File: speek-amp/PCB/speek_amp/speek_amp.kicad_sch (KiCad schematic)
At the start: 5 parts

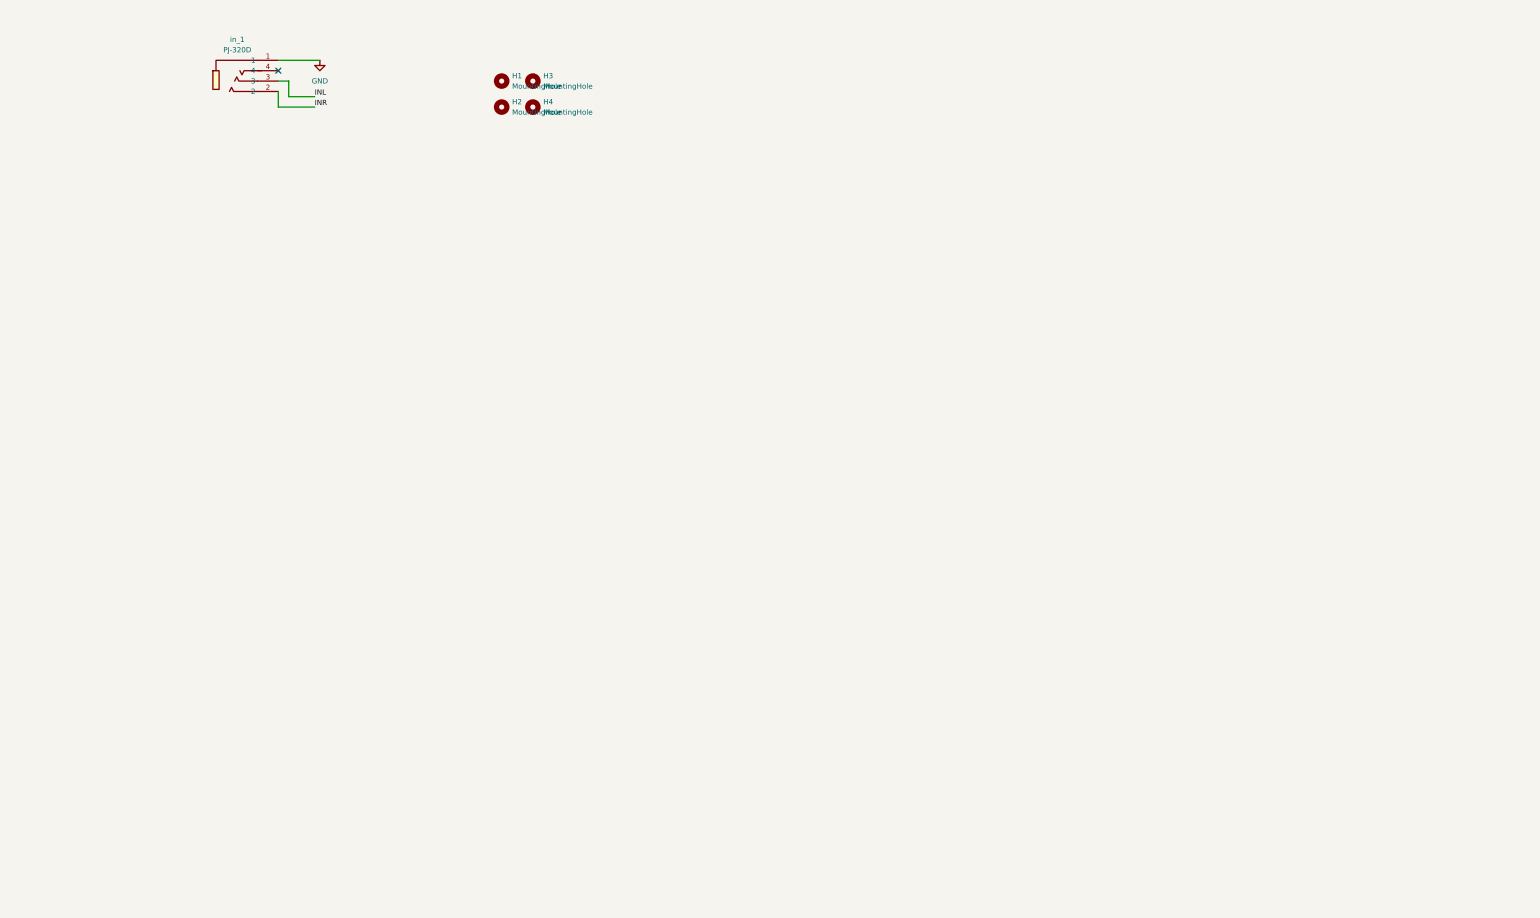
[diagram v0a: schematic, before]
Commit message: the speek amp schematic
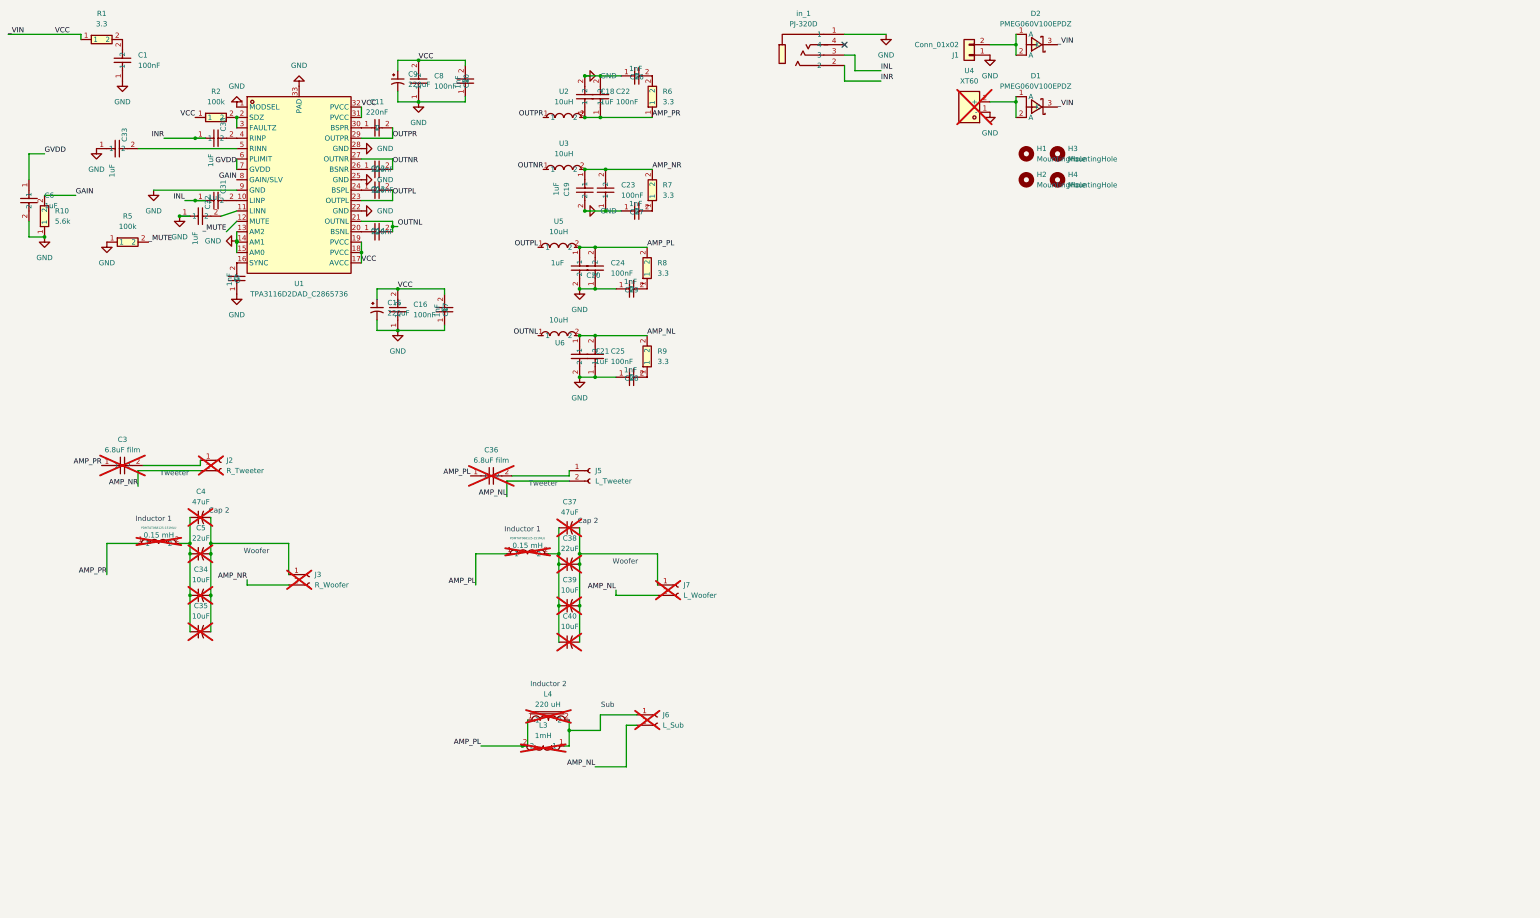
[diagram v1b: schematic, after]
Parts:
- added C1, C16, C22, C23, C24, C25, C8: 100nF, easyeda2kicad:C0402, symbol lcsc:CC0402KRX7R7BB104
- added C10, C17, C26, C27, C28, C29, C7: 1nF, easyeda2kicad:C0402, symbol lcsc:CL05B102KB5NNNC
- added C11, C12, C13, C14: 220nF, easyeda2kicad:C0402, symbol lcsc:CL05B224KO5NNNC
- added C15, C9: 220uF, easyeda2kicad:CAP-SMD_BD8.0-L8.3-W8.3-FD, symbol Device:C_Polarized_Small_US
- added C18, C19, C20, C21, C30, C31, C32, C33, C6: 1uF, easyeda2kicad:C0402, symbol lcsc:CGA0402X5R105M100GT
- added C3, C36: 6.8uF film, easyeda2kicad:CAP-TH_L29.5-W12.7-P27.00-D0.8, symbol lcsc:W312G685JS8SA1C0EC
- added C34, C35, C39, C40: 10uF, Capacitor_THT:CP_Radial_D6.3mm_P2.50mm, symbol Device:C_Small_US
- added C37, C4: 47uF, Capacitor_THT:CP_Radial_D6.3mm_P2.50mm, symbol Device:C_Small_US
- added C38, C5: 22uF, Capacitor_THT:CP_Radial_D6.3mm_P2.50mm, symbol Device:C_Small_US
- added D1, D2: PMEG060V100EPDZ, easyeda2kicad:SOT1289_L5.8-W4.4-LS6.5-RD, symbol lcsc:PMEG060V100EPDZ
- added J1: Conn_01x02, Connector_JST:JST_VH_B2P-VH-B_1x02_P3.96mm_Vertical, symbol Connector_Generic:Conn_01x02
- added J2: R_Tweeter, Connector_PinHeader_2.54mm:PinHeader_1x02_P2.54mm_Vertical, symbol Connector:Conn_01x02_Socket
- added J3: R_Woofer, Connector_PinHeader_2.54mm:PinHeader_1x02_P2.54mm_Vertical, symbol Connector:Conn_01x02_Socket
- added J5: L_Tweeter, Connector_PinHeader_2.54mm:PinHeader_1x02_P2.54mm_Vertical, symbol Connector:Conn_01x02_Socket
- added J6: L_Sub, Connector_PinHeader_2.54mm:PinHeader_1x02_P2.54mm_Vertical, symbol Connector:Conn_01x02_Socket
- added J7: L_Woofer, Connector_PinHeader_2.54mm:PinHeader_1x02_P2.54mm_Vertical, symbol Connector:Conn_01x02_Socket
- added L3: 1mH, easyeda2kicad:IND-TH_L33.0-W21.0-P15.3-D1.0, symbol lcsc:PDMTAT3321-102MLG
- added L4: 220 uH, easyeda2kicad:IND-TH_BD22.3-P8.50-D1.2_XR068125TS221MHL8, symbol lcsc:XR068125TS221MHL8
- added R1, R6, R7, R8, R9: 3.3, easyeda2kicad:R0402, symbol lcsc:RC0402FR-073R3L
- added R10: 5.6k, easyeda2kicad:R0805, symbol lcsc:0805W8F5601T5E
- added R2, R5: 100k, easyeda2kicad:R0402, symbol lcsc:RC0402FR-07100KL
- added U1: TPA3116D2DAD_C2865736, easyeda2kicad:HTSSOP-32_L11.0-W6.1-P0.65-LS8.1-BL, symbol lcsc:TPA3116D2DAD_C2865736
- added U2, U3, U5, U6: 10uH, easyeda2kicad:IND-SMD_L7.2-W6.6_GPSR07X0, symbol lcsc:CYA0630-10UH
- added U4: XT60, easyeda2kicad:CONN-TH_XT60, symbol lcsc:XT60
- added U7, U8: PDMTAT068125-151MLU, easyeda2kicad:IND-TH_L23.0-W12.0-P8.00-D0.8, symbol lcsc:PDMTAT068125-151MLU
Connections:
- net GND: now also C1.1, C10.1, C15.2, C16.1, C17.1, C18.2, C19.2, C20.2, C21.2, C22.2, C23.1, C24.1, C25.1, C26.1, C27.1, C28.1, C29.1, C32.1, C33.1, C6.2, C7.1, C8.1, C9.2, J1.1 (Pin_1), R10.1, R5.1, U1.1 (MODSEL), U1.13 (AM2), U1.14 (AM1), U1.15 (AM0), U1.22 (GND), U1.25 (GND), U1.28 (GND), U1.33 (PAD), U1.9 (GND), U4.1 (-)
- net INL: now also C31.1
- net INR: now also C30.1
- new net: C13.1, U1.24 (BSPL)
- new net: C34.2, C35.2, C4.2, C5.2, J3.1 (Pin_1)
- new net: D1.1 (A), D1.2 (A), U4.2 (+)
- new net: C14.1, U1.20 (BSNL)
- new net: D2.1 (A), D2.2 (A), J1.2 (Pin_2)
- new net: C28.2, R9.1
- new net: C1.2, R1.2
- new net: C37.1, C38.1, C39.1, C40.1, U8.2
- new net: C37.2, C38.2, C39.2, C40.2, J7.1 (Pin_1)
- new net: C34.1, C35.1, C4.1, C5.1, U7.2
- new net: C33.2, U1.5 (RINN)
- new net: C31.2, U1.10 (LINP)
- new net: C32.2, U1.11 (LINN)
- new net: C7.2, U1.16 (SYNC)
- new net: R2.2, U1.2 (SDZ), U1.3 (FAULTZ)
- new net: C12.1, U1.26 (BSNR)
- new net: C11.1, U1.30 (BSPR)
- new net: C30.2, U1.4 (RINP)
- new net: C3.2, J2.1 (Pin_1)
- new net: C27.2, R7.1
- new net: J6.1 (Pin_1), L3.1, L4.2
- new net: C29.2, R8.1
- new net: C26.2, R6.2
- new net: C36.2, J5.1 (Pin_1)
- new net AMP_NL: C21.1, C25.2, J5.2 (Pin_2), J6.2 (Pin_2), J7.2 (Pin_2), R9.2, U6.2
- new net AMP_NR: C19.1, C23.2, J2.2 (Pin_2), J3.2 (Pin_2), R7.2, U3.2
- new net AMP_PL: C20.1, C24.2, C36.1, L3.2, L4.1, R8.2, U5.2, U8.1
- new net AMP_PR: C18.1, C22.1, C3.1, R6.1, U2.2, U7.1
- new net GAIN: R10.2, U1.8 (GAIN/SLV)
- new net GVDD: C6.1, U1.6 (PLIMIT), U1.7 (GVDD)
- new net OUTNL: C14.2, U1.21 (OUTNL), U6.1
- new net OUTNR: C12.2, U1.27 (OUTNR), U3.1
- new net OUTPL: C13.2, U1.23 (OUTPL), U5.1
- new net OUTPR: C11.2, U1.29 (OUTPR), U2.1
- new net VCC: C10.2, C15.1, C16.2, C17.2, C8.2, C9.1, D1.3 (K), D2.3 (K), R1.1, R2.1, U1.17 (AVCC), U1.18 (PVCC), U1.19 (PVCC), U1.31 (PVCC), U1.32 (PVCC)
- new net _MUTE: R5.2, U1.12 (MUTE)
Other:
- note added: "Cap 2"
- note added: "Inductor 1"
- note added: "Inductor 2"
- note added: "Sub"
- note added: "Tweeter"
- note added: "Woofer"
- moved on the sheet: H1, H2, H3, H4, in_1

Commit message: a
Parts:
- added U9: 25PX4700MEFC16X25, easyeda2kicad:CAP-TH_BD16.0-P7.50-D1.2-FD, symbol lcsc:25PX4700MEFC16X25
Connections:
- net GND: now also U9.2
- net VCC: now also U9.1
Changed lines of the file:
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@@
 		)
 	)
+	(label "_VIN"
+		(at 292.1 27.94 180)
+		(effects
+			(font
+				(size 1.27 1.27)
+			)
+			(justify right bottom)
+		)
+	)
 	(label "AMP_PL"
 		(at 133.35 154.94 180)
@@
 	)
 	(symbol
+		(lib_id "power:GND")
+		(at 302.26 27.94 0)
+		(unit 1)
+		(body_style 1)
+		(exclude_from_sim no)
+		(in_bom yes)
+		(on_board yes)
+		(in_pos_files yes)
+		(dnp no)
+		(fields_autoplaced yes)
+		(property "Reference" "#PWR022"
+			(at 302.26 34.29 0)
+			(hide yes)
+			(show_name no)
+			(do_not_autoplace no)
+			(effects
+				(font
+					(size 1.27 1.27)
+				)
+			)
+		)
+		(property "Value" "GND"
+			(at 302.26 33.02 0)
+			(show_name no)
+			(do_not_autoplace no)
+			(effects
+				(font
+					(size 1.27 1.27)
+				)
+			)
+		)
+		(property "Footprint" ""
+			(at 302.26 27.94 0)
+			(hide yes)
+			(show_name no)
+			(do_not_autoplace no)
+			(effects
+				(font
+					(size 1.27 1.27)
+				)
+			)
+		)
+		(property "Datasheet" ""
+			(at 302.26 27.94 0)
+			(hide yes)
+			(show_name no)
+			(do_not_autoplace no)
+			(effects
+				(font
+					(size 1.27 1.27)
+				)
+			)
+		)
+		(property "Description" "Power symbol creates a global label with name \"GND\" , ground"
+			(at 302.26 27.94 0)
+			(hide yes)
+			(show_name no)
+			(do_not_autoplace no)
+			(effects
+				(font
+					(size 1.27 1.27)
+				)
+			)
+		)
+		(pin "1"
+		)
+		(instances
+			(project "speek_amp"
+				(path "/f44fef8a-a473-4113-8c2c-ab86f69ad3c3"
+					(reference "#PWR022")
+					(unit 1)
+				)
+			)
+		)
+	)
+	(symbol
 		(lib_id "lcsc:PMEG060V100EPDZ")
 		(at 270.51 38.1 270)
@@
 					(unit 1)
 				)
+			)
+		)
+	)
+	(symbol
+		(lib_id "lcsc:25PX4700MEFC16X25")
+		(at 297.18 27.94 0)
+		(unit 1)
+		(body_style 1)
+		(exclude_from_sim no)
+		(in_bom yes)
+		(on_board yes)
+		(in_pos_files yes)
+		(dnp no)
+		(fields_autoplaced yes)
+		(property "Reference" "U9"
+			(at 297.18 21.59 0)
+			(show_name no)
+			(do_not_autoplace no)
+			(effects
+				(font
+					(size 1.27 1.27)
+				)
+			)
+		)
+		(property "Value" "25PX4700MEFC16X25"
+			(at 297.18 24.13 0)
+			(show_name no)
+			(do_not_autoplace no)
+			(effects
+				(font
+					(size 1.27 1.27)
+				)
+			)
+		)
+		(property "Footprint" "easyeda2kicad:CAP-TH_BD16.0-P7.50-D1.2-FD"
+			(at 297.18 35.56 0)
+			(hide yes)
+			(show_name no)
+			(do_not_autoplace no)
+			(effects
+				(font
+					(size 1.27 1.27)
+				)
+			)
+		)
+		(property "Datasheet" "https://www.lcsc.com/datasheet/C1601148.pdf"
+			(at 297.18 38.1 0)
+			(hide yes)
+			(show_name no)
+			(do_not_autoplace no)
+			(effects
+				(font
+					(size 1.27 1.27)
+				)
+			)
+		)
+		(property "Description" ""
+			(at 297.18 27.94 0)
+			(hide yes)
+			(show_name no)
+			(do_not_autoplace no)
+			(effects
+				(font
+					(size 1.27 1.27)
+				)
+			)
+		)
+		(property "Manufacturer" "Rubycon(红宝石)"
+			(at 297.18 40.64 0)
+			(hide yes)
+			(show_name no)
+			(do_not_autoplace no)
+			(effects
+				(font
+					(size 1.27 1.27)
+				)
+			)
+		)
+		(property "MPN" "25PX4700MEFC16X25"
+			(at 297.18 43.18 0)
+			(hide yes)
+			(show_name no)
+			(do_not_autoplace no)
+			(effects
+				(font
+					(size 1.27 1.27)
+				)
+			)
+		)
+		(property "LCSC Part" "C1601148"
+			(at 297.18 45.72 0)
+			(hide yes)
+			(show_name no)
+			(do_not_autoplace no)
+			(effects
+				(font
+					(size 1.27 1.27)
+				)
+			)
+		)
+		(pin "1"
+		)
+		(pin "2"
+		)
+		(instances
+			(project "speek_amp"
+				(path "/f44fef8a-a473-4113-8c2c-ab86f69ad3c3"
+					(reference "U9")
+					(unit 1)
+				)
